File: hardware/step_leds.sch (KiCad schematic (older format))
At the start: 10 parts

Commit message: Minor adjustments to schematics before PCB
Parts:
- added C44: 100n, Capacitor_SMD:C_0603_1608Metric, symbol Device:C
- added J3: Conn_01x04, Connector_PinHeader_2.54mm:PinHeader_1x04_P2.54mm_Vertical, symbol Connector_Generic:Conn_01x04
- D1, D2, D3, D4, D5, D6, D7, D8: renamed from D?; value LED_Dual_CAC -> SSL-LX3059IGW-CA; footprint (none) -> LED_THT:LED_D3.0mm-3
- IC3: renamed from IC?; footprint SOP64P600X175-24N -> TLC59482DBQ:SOP64P600X175-24N
- R4: renamed from R?; footprint (none) -> Resistor_SMD:R_0603_1608Metric
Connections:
- net +5V is gone; now on net +3V3: D1.2 (A), D2.2 (A), D3.2 (A), D4.2 (A), D5.2 (A), D6.2 (A), D7.2 (A), D8.2 (A)
- net +3V3: now also C44.1
- net GND: now also C44.2
- net led_clk: now also J3.2 (Pin_2)
- net led_gsclk: now also J3.4 (Pin_4)
- net led_lat: now also J3.3 (Pin_3)
- net led_sin: now also J3.1 (Pin_1)
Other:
- note added: "Debug"

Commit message: Last adjustments to hardware before v0.1 release
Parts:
- C12: renamed from C44; LCSC (none) -> C14663; LCSC Part # (none) -> C14663
- R4: LCSC (none) -> C22975; LCSC Part # (none) -> C22975
- renumbered D8 to D2, D7 to D3, D6 to D4, D1 to D6, D2 to D7, D3 to D8, D4 to D9
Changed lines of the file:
@@
 $EndDescr
 $Comp
-L Device:LED_Dual_CAC D8
+L Device:LED_Dual_CAC D2
 U 1 1 5FDF6EDC
 P 3150 2350
-F 0 "D8" H 3150 2775 50  0000 C CNN
+F 0 "D2" H 3150 2775 50  0000 C CNN
 F 1 "SSL-LX3059IGW-CA" H 3150 2684 50  0000 C CNN
 F 2 "LED_THT:LED_D3.0mm-3" H 3200 2350 50  0001 C CNN
@@
 $EndComp
 $Comp
-L power:GND #PWR023
+L power:GND #PWR029
 U 1 1 5FDFDAF0
 P 4850 3200
-F 0 "#PWR023" H 4850 2950 50  0001 C CNN
+F 0 "#PWR029" H 4850 2950 50  0001 C CNN
 F 1 "GND" V 4855 3072 50  0000 R CNN
 F 2 "" H 4850 3200 50  0001 C CNN
@@
 led_gsclk
 $Comp
-L power:+3V3 #PWR024
+L power:+3V3 #PWR030
 U 1 1 5FDFE8DD
 P 6450 2900
-F 0 "#PWR024" H 6450 2750 50  0001 C CNN
+F 0 "#PWR030" H 6450 2750 50  0001 C CNN
 F 1 "+3V3" H 6465 3073 50  0000 C CNN
 F 2 "" H 6450 2900 50  0001 C CNN
@@
 F 2 "Resistor_SMD:R_0603_1608Metric" V 6680 3300 50  0001 C CNN
 F 3 "~" H 6750 3300 50  0001 C CNN
+F 4 "C22975" H 6750 3300 50  0001 C CNN "LCSC Part #"
+F 5 "C22975" H 6750 3300 50  0001 C CNN "LCSC"
 	1    6750 3300
 	0    1    1    0
@@
 	6450 3200 6450 2900
 $Comp
-L power:GND #PWR025
+L power:GND #PWR031
 U 1 1 5FE04150
 P 7050 3300
-F 0 "#PWR025" H 7050 3050 50  0001 C CNN
+F 0 "#PWR031" H 7050 3050 50  0001 C CNN
 F 1 "GND" V 7055 3172 50  0000 R CNN
 F 2 "" H 7050 3300 50  0001 C CNN
@@
 	2650 2350 2850 2350
 $Comp
-L Device:LED_Dual_CAC D7
+L Device:LED_Dual_CAC D3
 U 1 1 5FE11CB2
 P 3150 3250
-F 0 "D7" H 3150 3675 50  0000 C CNN
+F 0 "D3" H 3150 3675 50  0000 C CNN
 F 1 "SSL-LX3059IGW-CA" H 3150 3584 50  0000 C CNN
 F 2 "LED_THT:LED_D3.0mm-3" H 3200 3250 50  0001 C CNN
@@
 	2650 3250 2850 3250
 $Comp
-L Device:LED_Dual_CAC D6
+L Device:LED_Dual_CAC D4
 U 1 1 5FE125CF
 P 3150 4150
-F 0 "D6" H 3150 4575 50  0000 C CNN
+F 0 "D4" H 3150 4575 50  0000 C CNN
 F 1 "SSL-LX3059IGW-CA" H 3150 4484 50  0000 C CNN
 F 2 "LED_THT:LED_D3.0mm-3" H 3200 4150 50  0001 C CNN
@@
 	2650 5100 2850 5100
 $Comp
-L Device:LED_Dual_CAC D4
+L Device:LED_Dual_CAC D9
 U 1 1 5FE2E978
 P 8750 5100
-F 0 "D4" H 8750 5525 50  0000 C CNN
+F 0 "D9" H 8750 5525 50  0000 C CNN
 F 1 "SSL-LX3059IGW-CA" H 8750 5434 50  0000 C CNN
 F 2 "LED_THT:LED_D3.0mm-3" H 8800 5100 50  0001 C CNN
@@
 	9250 5100 9050 5100
 $Comp
-L Device:LED_Dual_CAC D3
+L Device:LED_Dual_CAC D8
 U 1 1 5FE2E985
 P 8750 4200
-F 0 "D3" H 8750 4625 50  0000 C CNN
+F 0 "D8" H 8750 4625 50  0000 C CNN
 F 1 "SSL-LX3059IGW-CA" H 8750 4534 50  0000 C CNN
 F 2 "LED_THT:LED_D3.0mm-3" H 8800 4200 50  0001 C CNN
@@
 	9250 4200 9050 4200
 $Comp
-L Device:LED_Dual_CAC D2
+L Device:LED_Dual_CAC D7
 U 1 1 5FE2E992
 P 8750 3300
-F 0 "D2" H 8750 3725 50  0000 C CNN
+F 0 "D7" H 8750 3725 50  0000 C CNN
 F 1 "SSL-LX3059IGW-CA" H 8750 3634 50  0000 C CNN
 F 2 "LED_THT:LED_D3.0mm-3" H 8800 3300 50  0001 C CNN
@@
 	9250 3300 9050 3300
 $Comp
-L Device:LED_Dual_CAC D1
+L Device:LED_Dual_CAC D6
 U 1 1 5FE2E99F
 P 8750 2350
-F 0 "D1" H 8750 2775 50  0000 C CNN
+F 0 "D6" H 8750 2775 50  0000 C CNN
 F 1 "SSL-LX3059IGW-CA" H 8750 2684 50  0000 C CNN
 F 2 "LED_THT:LED_D3.0mm-3" H 8800 2350 50  0001 C CNN
@@
 Debug
 $Comp
-L power:+3V3 #PWR0130
+L power:+3V3 #PWR023
 U 1 1 5FF6FC73
 P 2650 2350
-F 0 "#PWR0130" H 2650 2200 50  0001 C CNN
+F 0 "#PWR023" H 2650 2200 50  0001 C CNN
 F 1 "+3V3" H 2665 2523 50  0000 C CNN
 F 2 "" H 2650 2350 50  0001 C CNN
@@
 $EndComp
 $Comp
-L power:+3V3 #PWR0131
+L power:+3V3 #PWR024
 U 1 1 5FF70915
 P 2650 3250
-F 0 "#PWR0131" H 2650 3100 50  0001 C CNN
+F 0 "#PWR024" H 2650 3100 50  0001 C CNN
 F 1 "+3V3" H 2665 3423 50  0000 C CNN
 F 2 "" H 2650 3250 50  0001 C CNN
@@
 $EndComp
 $Comp
-L power:+3V3 #PWR0132
+L power:+3V3 #PWR025
 U 1 1 5FF70EC4
 P 2650 4150
-F 0 "#PWR0132" H 2650 4000 50  0001 C CNN
+F 0 "#PWR025" H 2650 4000 50  0001 C CNN
 F 1 "+3V3" H 2665 4323 50  0000 C CNN
 F 2 "" H 2650 4150 50  0001 C CNN
@@
 $EndComp
 $Comp
-L power:+3V3 #PWR0133
+L power:+3V3 #PWR026
 U 1 1 5FF716E0
 P 2650 5100
-F 0 "#PWR0133" H 2650 4950 50  0001 C CNN
+F 0 "#PWR026" H 2650 4950 50  0001 C CNN
 F 1 "+3V3" H 2665 5273 50  0000 C CNN
 F 2 "" H 2650 5100 50  0001 C CNN
@@
 $EndComp
 $Comp
-L power:+3V3 #PWR0134
+L power:+3V3 #PWR035
 U 1 1 5FF71B4D
 P 9250 5100
-F 0 "#PWR0134" H 9250 4950 50  0001 C CNN
+F 0 "#PWR035" H 9250 4950 50  0001 C CNN
 F 1 "+3V3" H 9265 5273 50  0000 C CNN
 F 2 "" H 9250 5100 50  0001 C CNN
@@
 $EndComp
 $Comp
-L power:+3V3 #PWR0135
+L power:+3V3 #PWR034
 U 1 1 5FF723C2
 P 9250 4200
-F 0 "#PWR0135" H 9250 4050 50  0001 C CNN
+F 0 "#PWR034" H 9250 4050 50  0001 C CNN
 F 1 "+3V3" H 9265 4373 50  0000 C CNN
 F 2 "" H 9250 4200 50  0001 C CNN
@@
 $EndComp
 $Comp
-L power:+3V3 #PWR0136
+L power:+3V3 #PWR033
 U 1 1 5FF73083
 P 9250 3300
-F 0 "#PWR0136" H 9250 3150 50  0001 C CNN
+F 0 "#PWR033" H 9250 3150 50  0001 C CNN
 F 1 "+3V3" H 9265 3473 50  0000 C CNN
 F 2 "" H 9250 3300 50  0001 C CNN
@@
 $EndComp
 $Comp
-L power:+3V3 #PWR0137
+L power:+3V3 #PWR032
 U 1 1 5FF737FE
 P 9250 2350
-F 0 "#PWR0137" H 9250 2200 50  0001 C CNN
+F 0 "#PWR032" H 9250 2200 50  0001 C CNN
 F 1 "+3V3" H 9265 2523 50  0000 C CNN
 F 2 "" H 9250 2350 50  0001 C CNN
@@
 P 3950 1350
 AR Path="/5FF3BC19" Ref="C?"  Part="1"
-AR Path="/5FDF6408/5FF3BC19" Ref="C44"  Part="1"
-F 0 "C44" H 4065 1396 50  0000 L CNN
+AR Path="/5FDF6408/5FF3BC19" Ref="C12"  Part="1"
+F 0 "C12" H 4065 1396 50  0000 L CNN
 F 1 "100n" H 4065 1305 50  0000 L CNN
 F 2 "Capacitor_SMD:C_0603_1608Metric" H 3988 1200 50  0001 C CNN
 F 3 "~" H 3950 1350 50  0001 C CNN
+F 4 "C14663" H 3950 1350 50  0001 C CNN "LCSC Part #"
+F 5 "C14663" H 3950 1350 50  0001 C CNN "LCSC"
 	1    3950 1350
 	1    0    0    -1
@@
 AR Path="/5FDE753F/5FF3BC31" Ref="#PWR?"  Part="1"
 AR Path="/5FF3BC31" Ref="#PWR?"  Part="1"
-AR Path="/5FDF6408/5FF3BC31" Ref="#PWR019"  Part="1"
-F 0 "#PWR019" H 3950 1050 50  0001 C CNN
+AR Path="/5FDF6408/5FF3BC31" Ref="#PWR027"  Part="1"
+F 0 "#PWR027" H 3950 1050 50  0001 C CNN
 F 1 "+3V3" V 3965 1328 50  0000 L CNN
 F 2 "" H 3950 1200 50  0001 C CNN
@@
 P 3950 1500
 AR Path="/5FF3BC37" Ref="#PWR?"  Part="1"
-AR Path="/5FDF6408/5FF3BC37" Ref="#PWR020"  Part="1"
-F 0 "#PWR020" H 3950 1250 50  0001 C CNN
+AR Path="/5FDF6408/5FF3BC37" Ref="#PWR028"  Part="1"
+F 0 "#PWR028" H 3950 1250 50  0001 C CNN
 F 1 "GND" H 3955 1327 50  0000 C CNN
 F 2 "" H 3950 1500 50  0001 C CNN

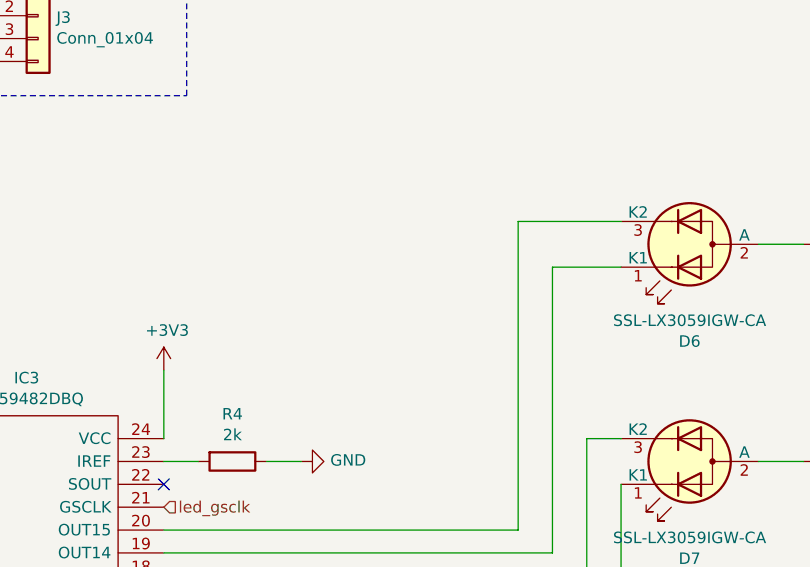
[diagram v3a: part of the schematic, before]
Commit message: Implement LED state and set function
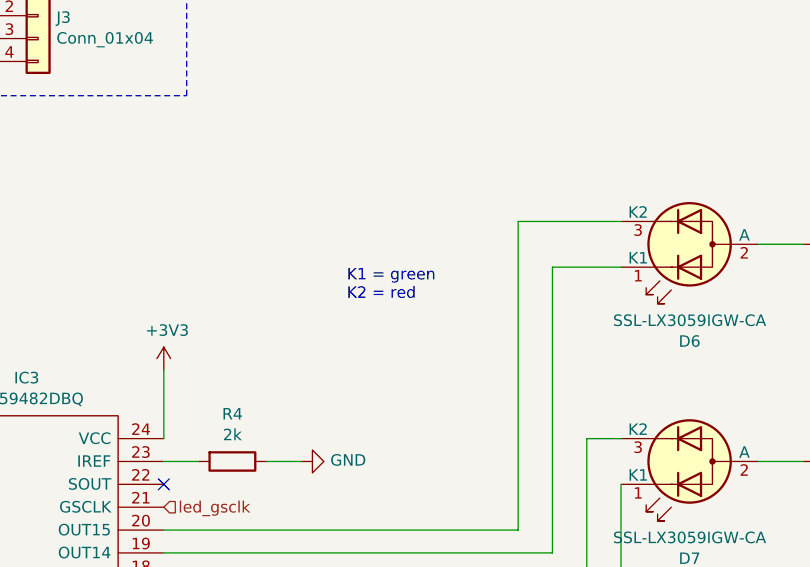
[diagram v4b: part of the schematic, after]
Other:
- note added: "K1 = green\nK2 = red"
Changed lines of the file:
@@
 	1    0    0    -1
 $EndComp
+Text Notes 7250 2600 0    50   ~ 0
+K1 = green\nK2 = red
 $EndSCHEMATC
